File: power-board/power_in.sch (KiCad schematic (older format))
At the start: 14 parts, among them U1 SPV1040

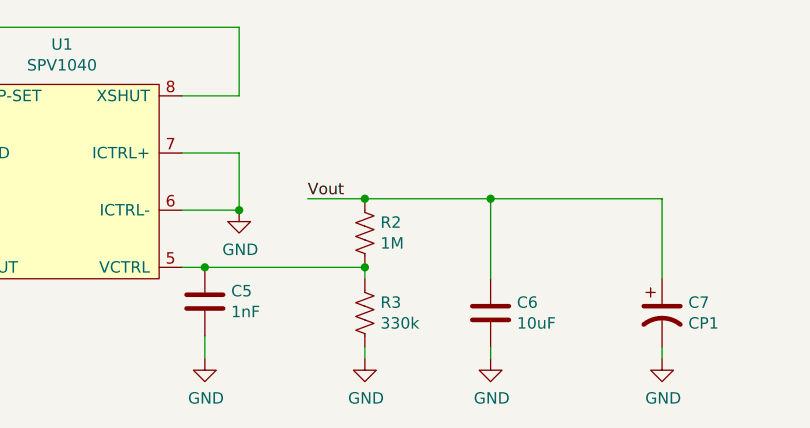
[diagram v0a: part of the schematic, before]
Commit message: Updated schematics to reflect new resistor values
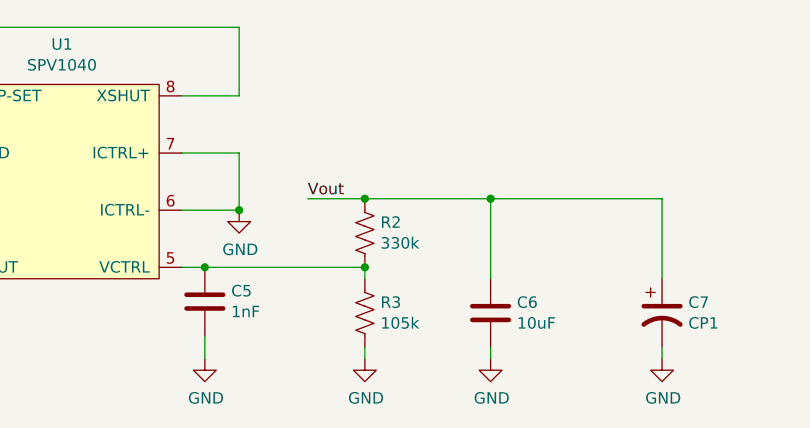
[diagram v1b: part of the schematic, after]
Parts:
- R2: value 1M -> 330k
- R3: value 330k -> 105k
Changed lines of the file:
@@
 P 7100 3800
 F 0 "R2" H 7168 3846 50  0000 L CNN
-F 1 "1M" H 7168 3755 50  0000 L CNN
+F 1 "330k" H 7168 3755 50  0000 L CNN
 F 2 "" V 7140 3790 50  0001 C CNN
 F 3 "~" H 7100 3800 50  0001 C CNN
@@
 P 7100 4150
 F 0 "R3" H 7168 4196 50  0000 L CNN
-F 1 "330k" H 7168 4105 50  0000 L CNN
+F 1 "105k" H 7168 4105 50  0000 L CNN
 F 2 "" V 7140 4140 50  0001 C CNN
 F 3 "~" H 7100 4150 50  0001 C CNN
